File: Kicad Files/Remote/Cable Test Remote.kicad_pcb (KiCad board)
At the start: 2 copper layers, 25.4 x 96.5 mm, 23 parts, among them J1 RJ45, J2 RJ12

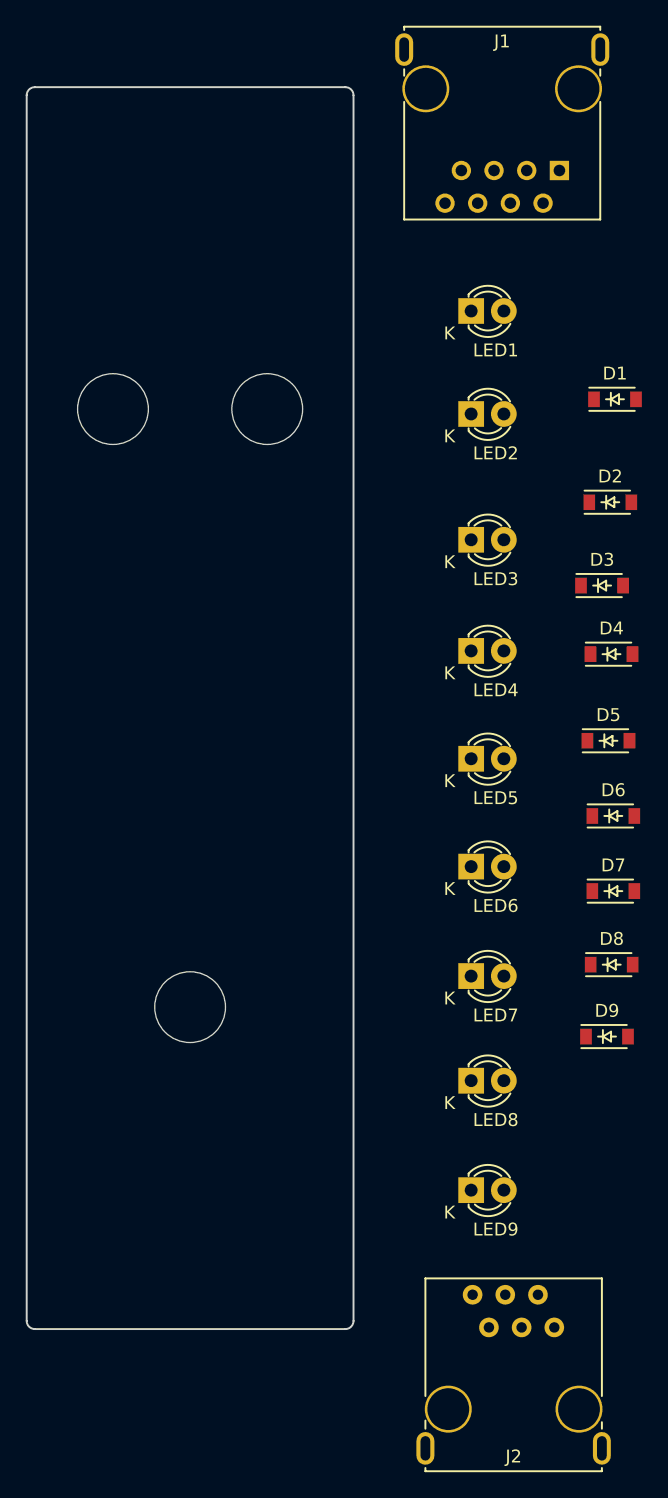
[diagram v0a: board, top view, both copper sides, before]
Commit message: Update Component Positioning on Master PCB
Updates the positioning of components to fix positioning issues introduced
by the earlier shortening of the board to improve fit.
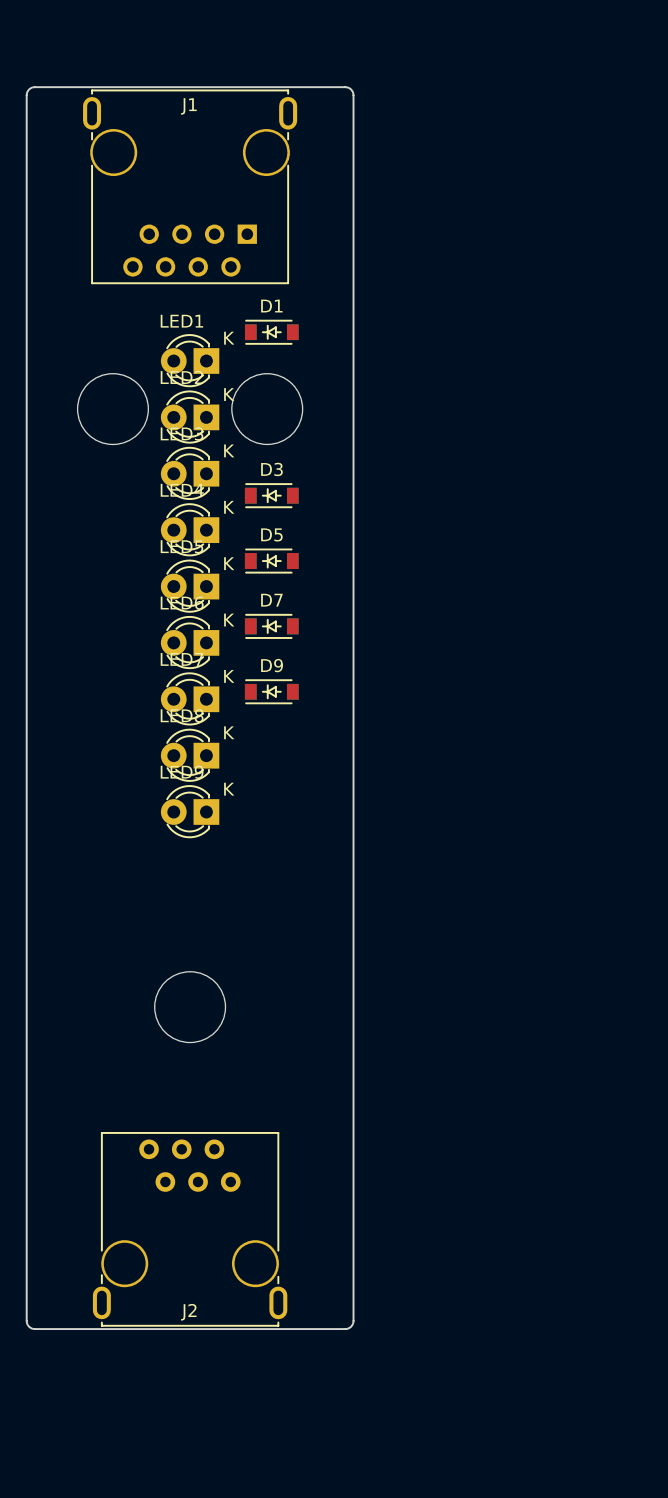
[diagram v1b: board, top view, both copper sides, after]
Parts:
- D2, D4, D6, D8: moved to B.Cu
- moved D9 37.4 mm to (120.7, 97.8)
- moved LED9 35.9 mm to (115.6, 107.1), turned to 180 degrees
- moved D8 33.9 mm to (120.7, 97.8)
- moved D7 33.6 mm to (120.7, 92.7)
- moved LED8 32.6 mm to (115.6, 102.8), turned to 180 degrees
- moved D6 30.4 mm to (120.7, 92.7)
- moved LED7 29.8 mm to (115.6, 98.4), turned to 180 degrees
- moved D5 29.7 mm to (120.7, 87.6)
- moved J2 27.6 mm to (114.3, 142.2)
- moved D4 27.4 mm to (120.7, 87.6)
- moved D1 27.2 mm to (120.7, 69.8)
- moved LED6 26.9 mm to (115.6, 94.0), turned to 180 degrees
- moved D3 26.6 mm to (120.7, 82.5)
- moved D2 26.3 mm to (120.7, 82.5)
- moved J1 24.8 mm to (114.3, 55.9)
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
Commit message: Perform initial trace routing for remote end PCB
Adds traces to PCB design for the remote end of the cable tester.
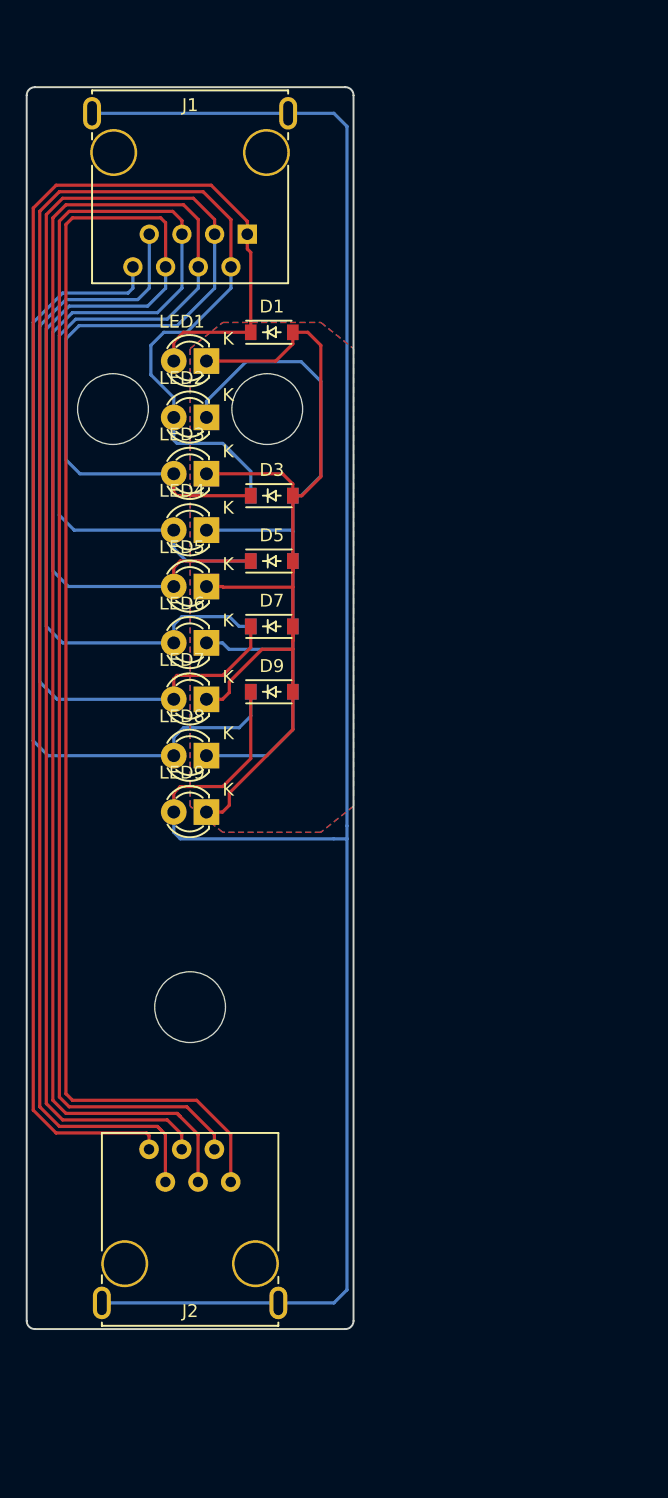
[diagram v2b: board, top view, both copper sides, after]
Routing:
- net /S: track 0.00 -> 159.1 mm
- net /6: track 0.00 -> 150.7 mm
- net /4: track 0.00 -> 145.9 mm
- net /5: track 0.00 -> 145.4 mm
- net /3: track 0.00 -> 140.3 mm
- net Net-(D1-Pad2): track 0.00 -> 139.1 mm
- net /2: track 0.00 -> 131.0 mm
- net /1: track 0.00 -> 116.4 mm
- net /8: track 0.00 -> 64.4 mm
- net /7: track 0.00 -> 62.8 mm
- added copper zone on B.Cu, net Net-(D1-Pad2)
- added copper zone on F.Cu, net Net-(D1-Pad2)

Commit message: Adjust trace width and add text to remote end PCB
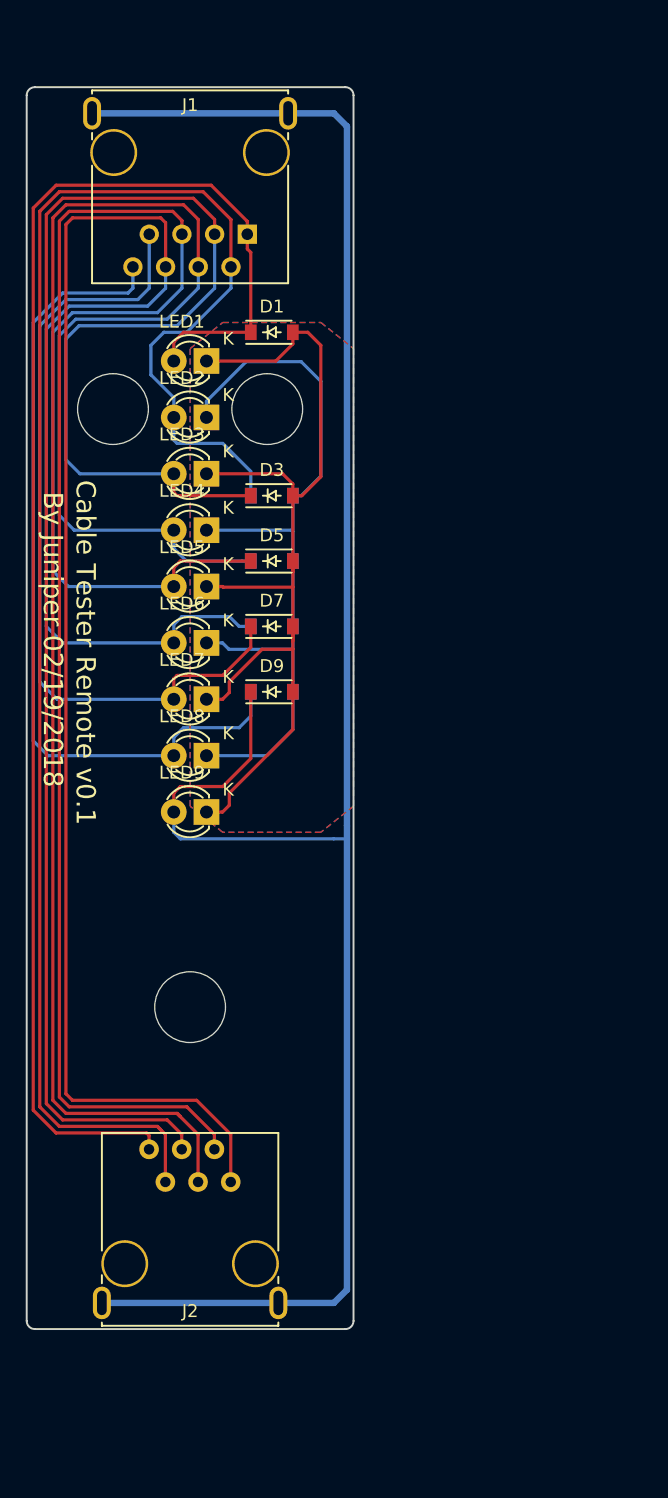
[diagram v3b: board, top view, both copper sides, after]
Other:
- board text added: "By Juniper 02/19/2018"
- board text added: "Cable Tester Remote v0.1"
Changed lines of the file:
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@@
     (links 44)
     (no_connects 0)
-    (area 101.524999 50.724999 127.075001 147.395001)
+    (area 99.721076 50.724999 128.878924 147.395001)
     (thickness 1.6)
-    (drawings 8)
+    (drawings 10)
     (tracks 214)
     (zones 0)
@@
     (fp_circle (center 0 0) (end 5.5 0) (layer Cmts.User) (width 0.381))
     (pad 1 thru_hole circle (at 0 0) (size 5.5 5.5) (drill 5.5) (layers))
+  )
+  (gr_text "By Juniper 02/19/2018" (at 103.632 93.726 270) (layer F.SilkS)
+    (effects (font (size 1.5 1.5) (thickness 0.3)))
+  )
+  (gr_text "Cable Tester Remote v0.1" (at 106.172 94.742 270) (layer F.SilkS)
+    (effects (font (size 1.5 1.5) (thickness 0.3)))
   )
   (gr_line (start 101.6 146.685) (end 101.6 51.435) (layer Edge.Cuts) (width 0.15))
@@
   (segment (start 118.11 100.584) (end 119.015 99.679) (width 0.25) (layer B.Cu) (net 9))
   (segment (start 119.015 99.679) (end 119.015 97.79) (width 0.25) (layer B.Cu) (net 9))
-  (segment (start 121.92 52.832) (end 106.68 52.832) (width 0.25) (layer B.Cu) (net 10))
-  (segment (start 126.492 144.272) (end 126.492 109.22) (width 0.25) (layer B.Cu) (net 10))
-  (segment (start 126.492 109.22) (end 126.492 108.204) (width 0.25) (layer B.Cu) (net 10))
+  (segment (start 121.92 52.832) (end 106.68 52.832) (width 0.5) (layer B.Cu) (net 10))
+  (segment (start 126.492 144.272) (end 126.492 109.22) (width 0.5) (layer B.Cu) (net 10))
+  (segment (start 126.492 109.22) (end 126.492 108.204) (width 0.5) (layer B.Cu) (net 10))
   (segment (start 125.476 109.22) (end 126.492 109.22) (width 0.25) (layer B.Cu) (net 10))
-  (segment (start 125.476 145.288) (end 126.492 144.272) (width 0.25) (layer B.Cu) (net 10))
-  (segment (start 121.158 145.288) (end 125.476 145.288) (width 0.25) (layer B.Cu) (net 10))
-  (segment (start 107.442 145.288) (end 121.158 145.288) (width 0.25) (layer B.Cu) (net 10))
+  (segment (start 125.476 145.288) (end 126.492 144.272) (width 0.5) (layer B.Cu) (net 10))
+  (segment (start 121.158 145.288) (end 125.476 145.288) (width 0.5) (layer B.Cu) (net 10))
+  (segment (start 107.442 145.288) (end 121.158 145.288) (width 0.5) (layer B.Cu) (net 10))
   (segment (start 113.538 109.22) (end 113.03 108.712) (width 0.25) (layer B.Cu) (net 10))
   (segment (start 113.03 108.712) (end 113.03 107.1372) (width 0.25) (layer B.Cu) (net 10))
   (segment (start 125.476 109.22) (end 113.538 109.22) (width 0.25) (layer B.Cu) (net 10))
-  (segment (start 126.492 53.848) (end 126.492 108.204) (width 0.25) (layer B.Cu) (net 10))
-  (segment (start 125.476 52.832) (end 126.492 53.848) (width 0.25) (layer B.Cu) (net 10))
-  (segment (start 121.92 52.832) (end 125.476 52.832) (width 0.25) (layer B.Cu) (net 10))
+  (segment (start 126.492 53.848) (end 126.492 108.204) (width 0.5) (layer B.Cu) (net 10))
+  (segment (start 125.476 52.832) (end 126.492 53.848) (width 0.5) (layer B.Cu) (net 10))
+  (segment (start 121.92 52.832) (end 125.476 52.832) (width 0.5) (layer B.Cu) (net 10))
   (segment (start 113.538 105.156) (end 113.03 105.664) (width 0.25) (layer F.Cu) (net 10))
   (segment (start 113.03 105.664) (end 113.03 107.1372) (width 0.25) (layer F.Cu) (net 10))
